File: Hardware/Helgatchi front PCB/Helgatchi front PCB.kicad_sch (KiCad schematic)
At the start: 29 parts, among them J1 BATTERY, J2 SCREEN, M1 MOTOR, Q1 NMOS, Q2 NMOS, SW1 LEFT BUTTON, SW2 CENTER BUTTON, SW3 RIGHT BUTTON, U1 XIAO ESP32-S3

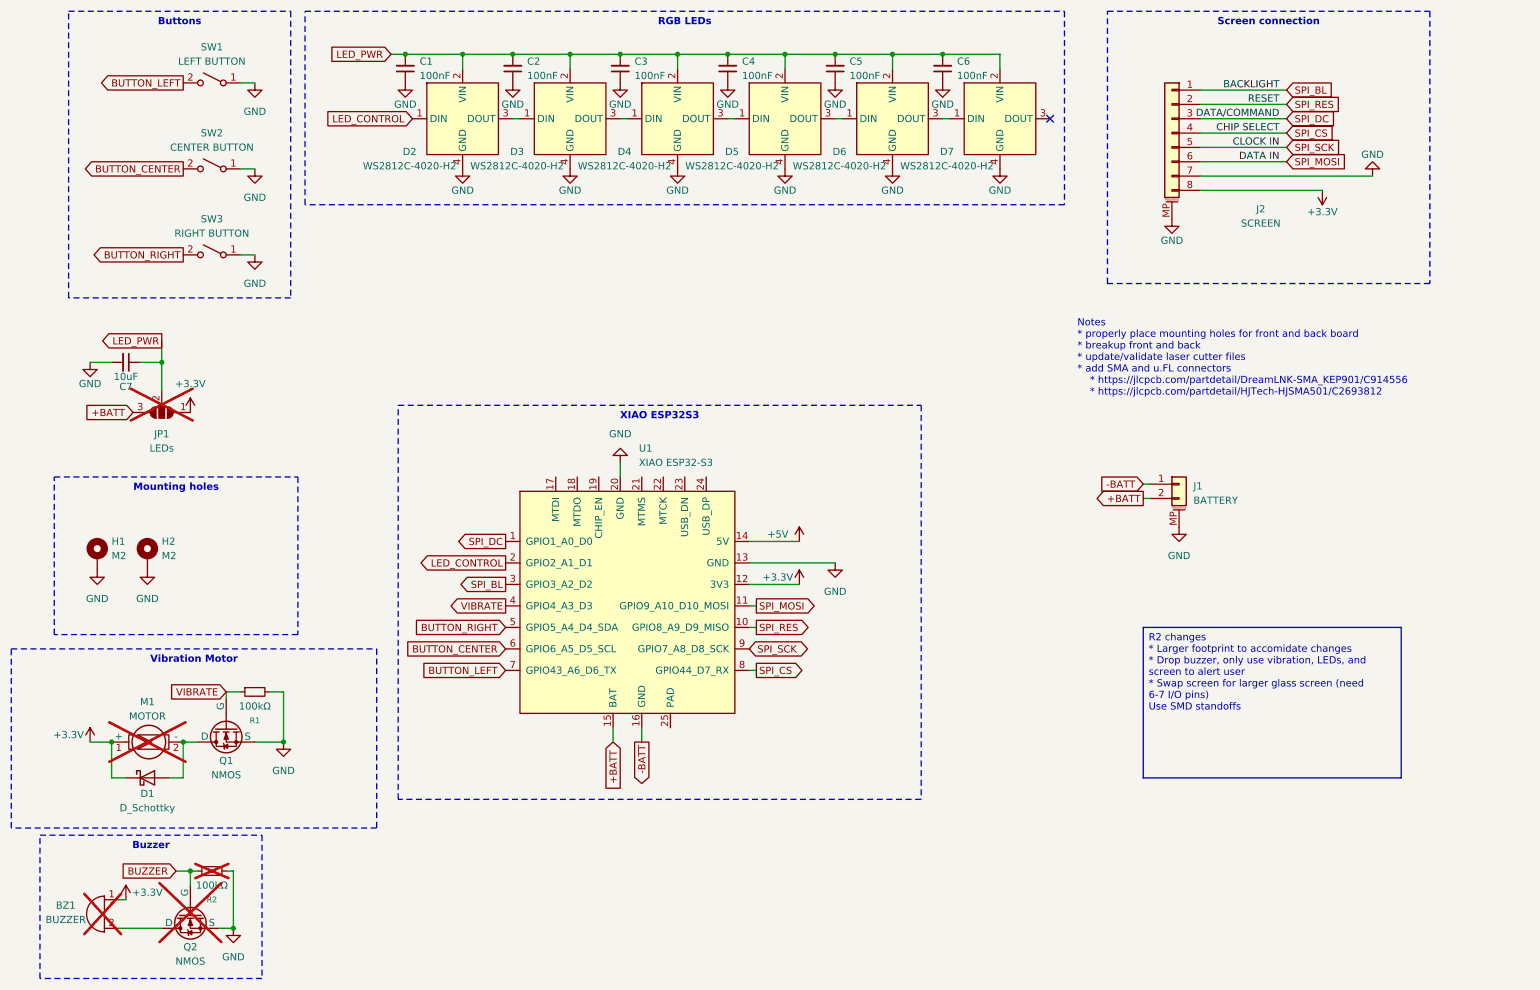
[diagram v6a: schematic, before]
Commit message: R2.7
- Shifted buttons up a tiny bit
- Made room for the vibration motor to be adhered to the PCB
- Enlarged vibration motor pads for easier hand soldering
- Removed LED voltage selector (now 3.3v)
- Removed unused pins from schematic and ESP32 footprint
- Added a keepout area under ESP32
- Replaced +BATT trace
- Removed -BATT trace, tied to GND
- Added keepout around button GND vias, to prevent heat soak during soldering
- Scooted ESP back a little bit to make room for assembly
- Adjusted front silkscreen
- Swapped buttons to two GPIO Diode matrix
- Added VSENSE + resistors and capacitor
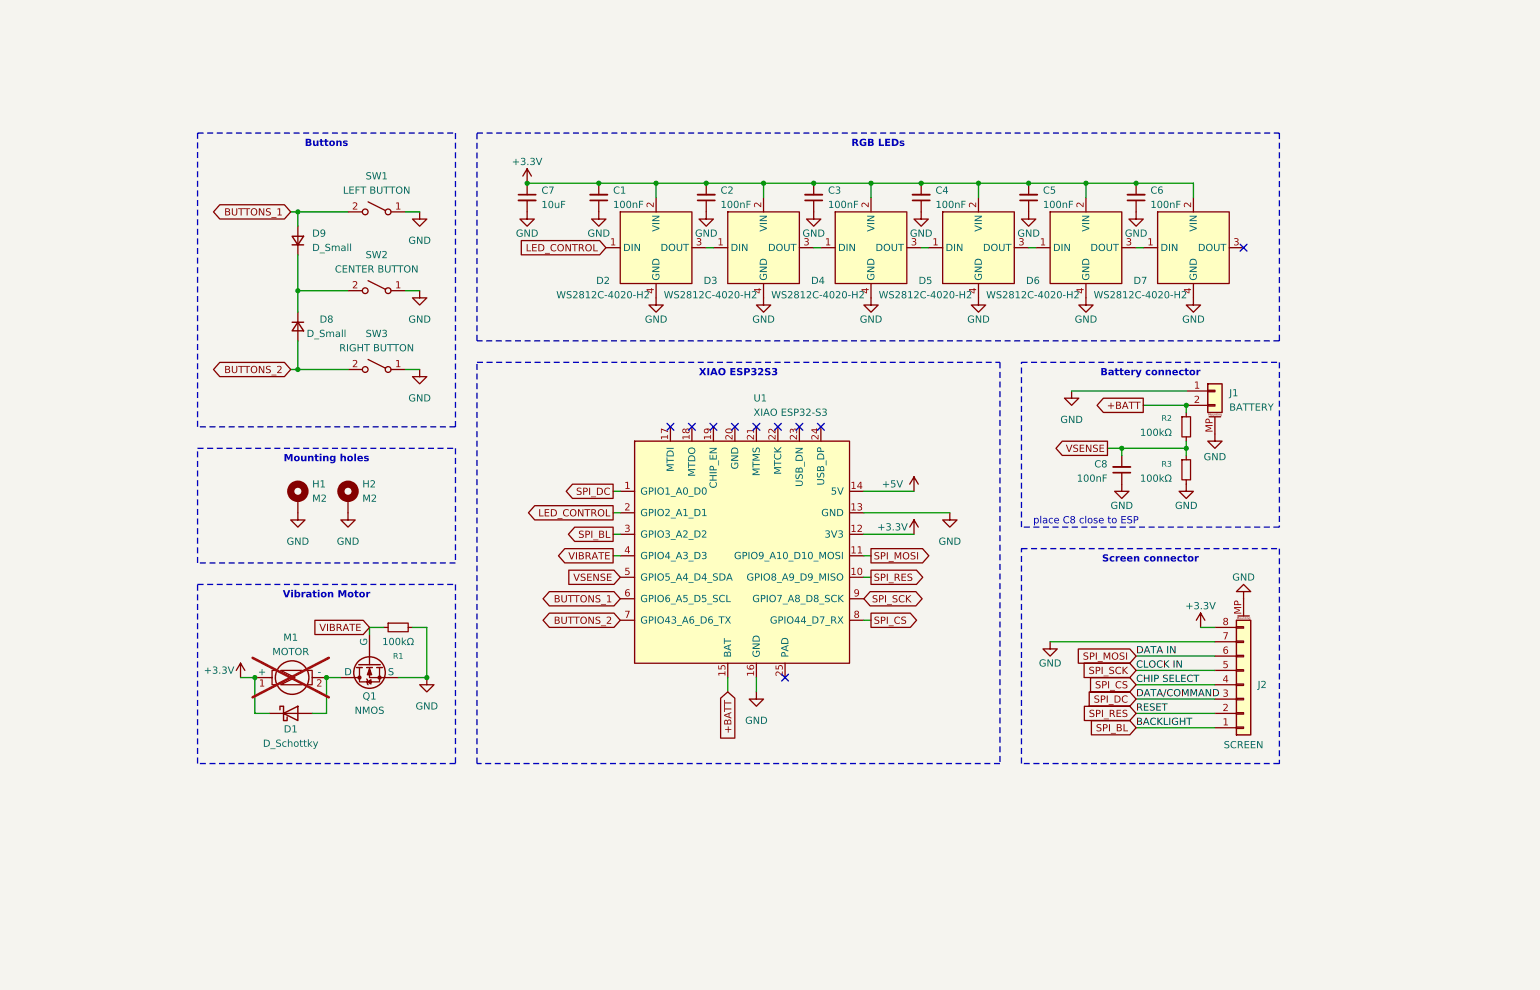
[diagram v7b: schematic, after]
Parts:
- removed BZ1: BUZZER, Connector_PinHeader_2.54mm:PinHeader_1x02_P2.54mm_Vertical, symbol Device:Buzzer
- removed JP1: LEDs, Jumper:SolderJumper-3_P1.3mm_Open_RoundedPad1.0x1.5mm_NumberLabels, symbol Jumper:SolderJumper_3_Open
- removed Q2: NMOS, Package_TO_SOT_SMD:SOT-23, symbol Simulation_SPICE:NMOS
- added C8: 100nF, Capacitor_SMD:C_0603_1608Metric, symbol Device:C_Small
- added D8, D9: D_Small, Diode_SMD:D_0603_1608Metric, symbol Device:D_Small
- added R3: 100kΩ, Resistor_SMD:R_0603_1608Metric, symbol Device:R_Small
- M1: LCSC Part # (none) -> C2682302; now in the parts list
- R2: now fitted; now in the parts list
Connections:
- net -BATT is gone; now on net GND: J1.1 (Pin_1), U1.16 (GND)
- net BUZZER is gone; now on net +BATT: R2.1
- net LED_PWR is gone; now on net +3.3V: C1.2, C2.2, C3.2, C4.2, C5.2, C6.2, C7.1, D2.2 (VIN), D3.2 (VIN), D4.2 (VIN), D5.2 (VIN), D6.2 (VIN), D7.2 (VIN)
- net GND: now also C8.1, R3.2; no longer R2.2, U1.20 (GND)
- net BUTTON_CENTER: no longer names the net of SW2.2 (B)
- net BUTTON_CENTER: now also D8.1 (K), D9.1 (K); no longer U1.6 (GPIO6_A5_D5_SCL)
- net BUTTON_LEFT renamed BUTTONS_1
- net BUTTONS_1: now also U1.6 (GPIO6_A5_D5_SCL), D9.2 (A); no longer U1.7 (GPIO43_A6_D6_TX)
- net BUTTON_RIGHT renamed BUTTONS_2
- net BUTTONS_2: now also U1.7 (GPIO43_A6_D6_TX), D8.2 (A); no longer U1.5 (GPIO5_A4_D4_SDA)
- new net VSENSE: C8.2, R2.2, R3.1, U1.5 (GPIO5_A4_D4_SDA)
- no-connect marks 1 -> 10
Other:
- note added: "place C8 close to ESP"
- note removed: "Notes * properly place mounting holes for front and back board * breakup front and back * update/validate laser cutter files * add SMA and u.FL connectors * https://jlcpcb.com/partdetail/DreamLNK-SMA_KEP901/C914556 * https://jlcpcb.com/partdetail/HJTech-HJSMA501/C2693812"
- company: (none) -> DC801 and Friends
- title: (none) -> Helgatchi Front PCB
- moved on the sheet: C1, C2, C3, C4, C5, C6, D1, D2, D3, D4, D5, D6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

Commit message: Wrap up R2.7
- Added voltage sensing
- made room for Vibration buzzer
- added SMD M2 nut
- swapped flyback diode
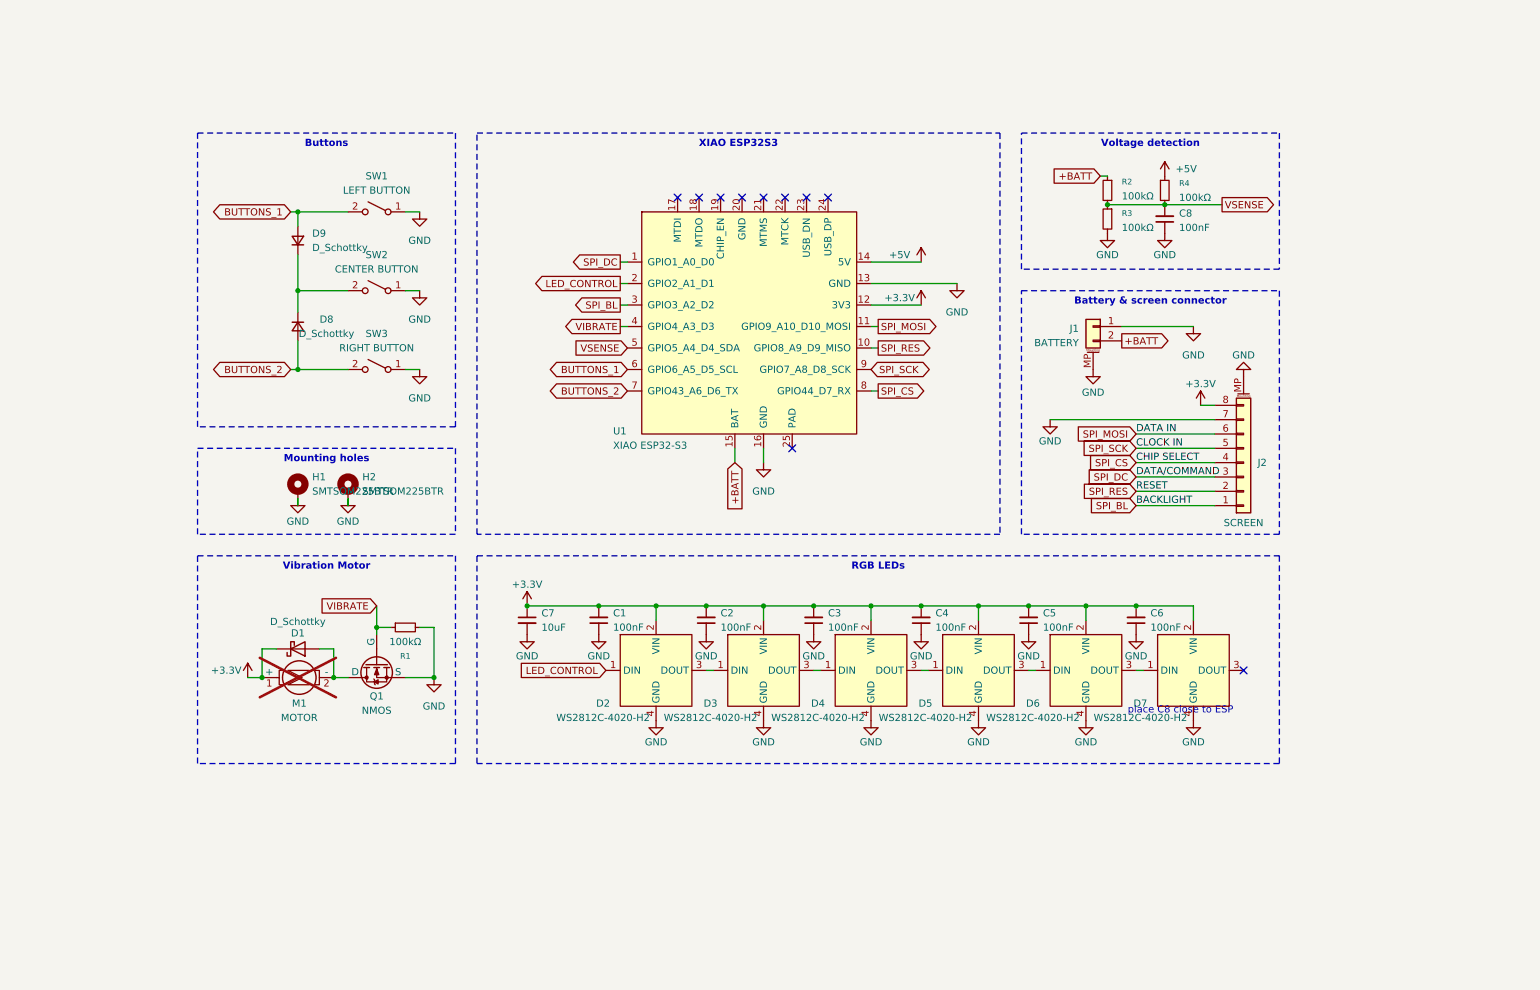
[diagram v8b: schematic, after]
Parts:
- added R4: 100kΩ, Resistor_SMD:R_0603_1608Metric, symbol Device:R_Small
- D1: footprint SDM2U30CSP:SDM2U30CSP -> Diode_SMD:D_SOD-523; LCSC Part # C35621074 -> C25803
- D8, D9: value D_Small -> D_Schottky; footprint Diode_SMD:D_0603_1608Metric -> Diode_SMD:D_SOD-523; LCSC Part # (none) -> C25803
- H1, H2: value M2 -> SMTSOM225BTR; footprint Mounting_Wuerth:Mounting_Wuerth_WA-SMSI-M2_H8mm_9774080243 -> SMTSOM225BTR:SMD_BD5.6-D3.6; LCSC Part # (none) -> C5301773
- R1, R2, R3: LCSC Part # (none) -> C25803
- SW1, SW2, SW3: LCSC Part # (none) -> C9900250000
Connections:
- net +5V: now also R4.1
- net VSENSE: now also R4.2
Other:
- moved on the sheet: C1, C2, C3, C4, C5, C6, C7, C8, D1, D2, D3, D4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
